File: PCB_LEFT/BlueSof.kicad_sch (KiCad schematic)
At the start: 88 parts, among them J1 USB_C_Receptacle_USB2.0, J12 SM02B-SRSS-TB(LF)(SN), Q2 A03407, SW1 SW_PUSH, SW10 SW_PUSH, SW11 SW_PUSH, SW12 SW_PUSH, SW13 SW_PUSH, SW14 SW_PUSH, SW15 SW_PUSH, SW16 SW_PUSH, SW17 SW_PUSH, SW18 SW_PUSH, SW19 SW_PUSH, SW2 SW_PUSH, SW20 SW_PUSH, SW21 SW_PUSH, SW22 SW_PUSH, SW23 SW_PUSH, SW24 SW_PUSH, SW25 Rotary_Encoder_Switch, SW26 SW_PUSH, SW27 SW_PUSH, SW28 SW_PUSH, SW3 SW_PUSH, SW4 SW_PUSH, SW5 SW_PUSH, SW6 SW_PUSH, SW7 SW_PUSH, SW8 SW_PUSH, SW9 SW_PUSH, U1 LN2054Y42AMR, U2 E73-2G4M08S1C, U3 AP2112K-3.3, Y1 32.768kHz

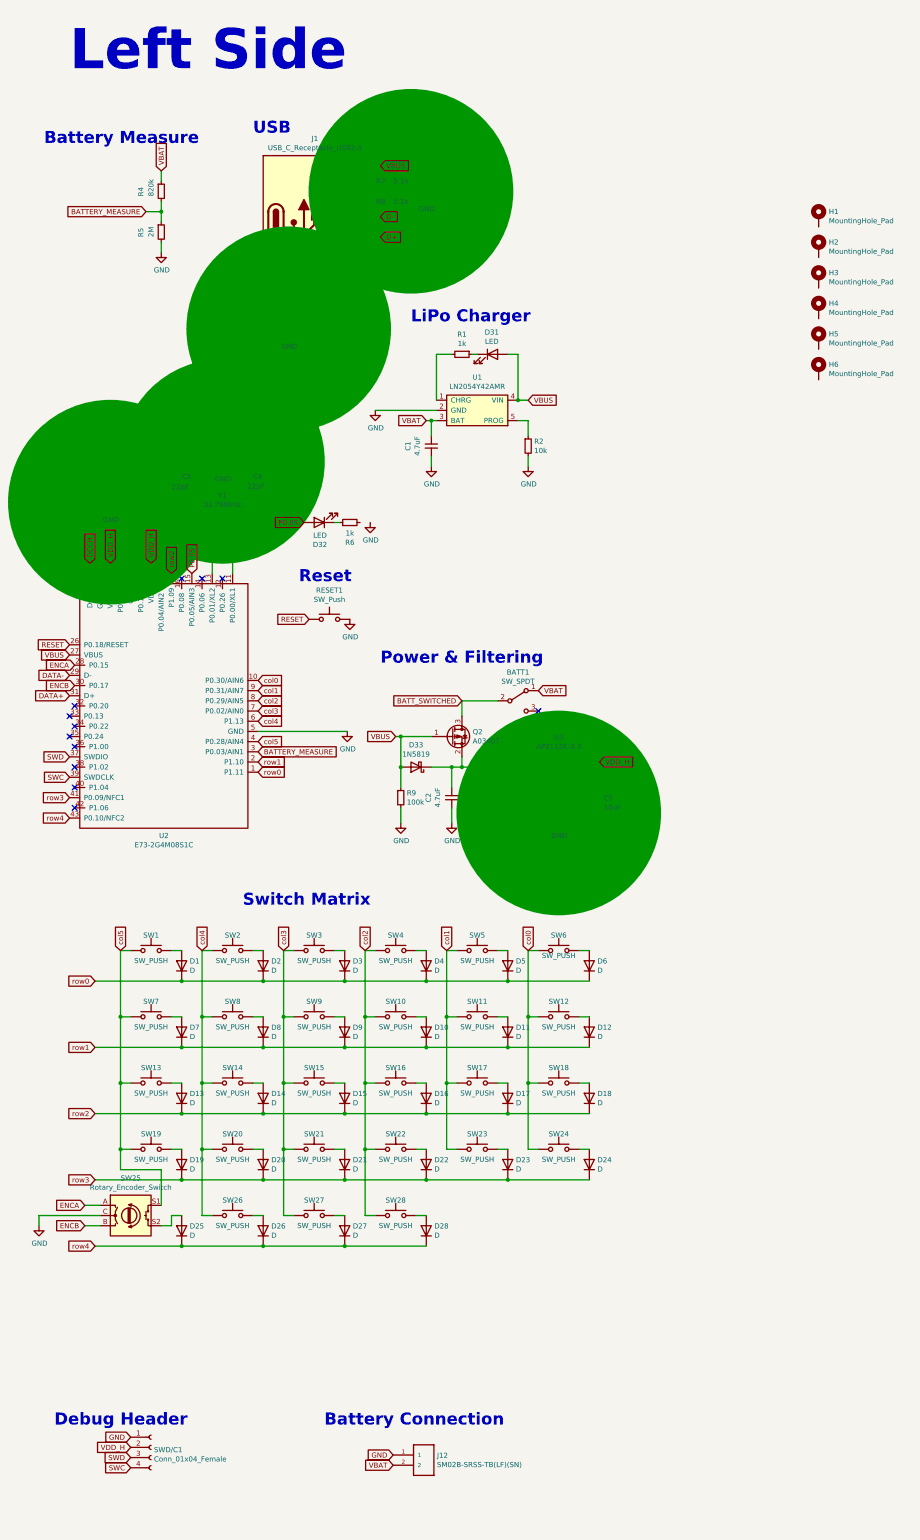
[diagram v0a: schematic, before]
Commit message: ordered left side from jlc
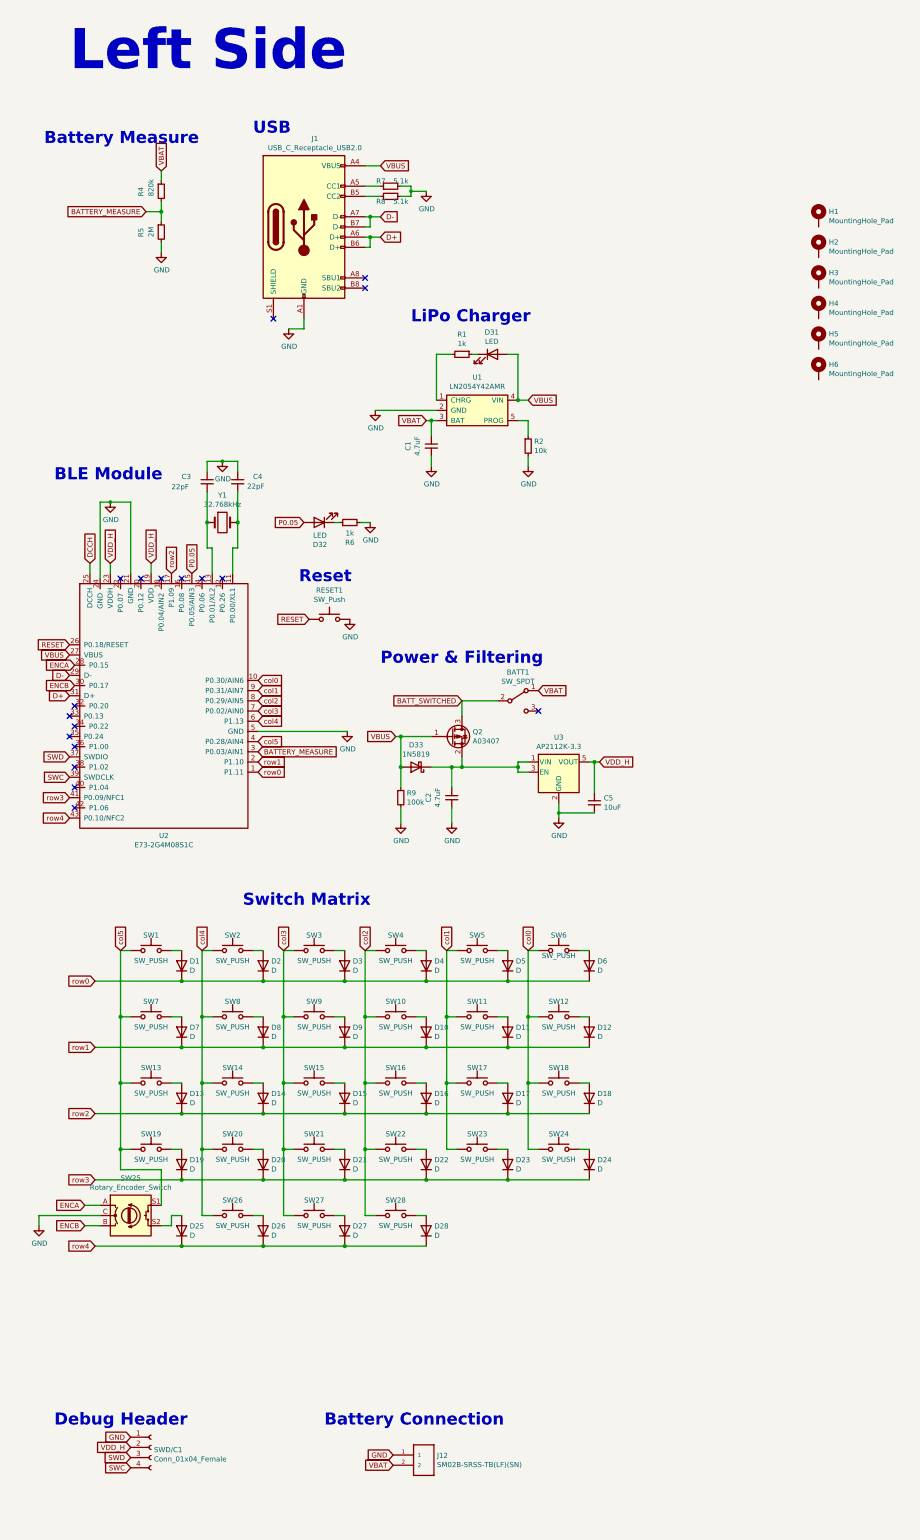
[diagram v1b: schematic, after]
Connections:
- net DATA+ is gone; now on net D+: U2.31 (D+)
- net DATA- is gone; now on net D-: U2.29 (D-)
- net GND: now also R6.2; no longer J1.S1 (SHIELD)
- no-connect marks 17 -> 18
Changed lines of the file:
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@@
     (rev "R1")
   )
-  (junction (at 325.12 146.05) (diameter 50.9956) (color 0 0 0 0))
+  (junction (at 325.12 146.05) (diameter 0.9144) (color 0 0 0 0))
   (junction (at 327.66 274.32) (diameter 1.016) (color 0 0 0 0))
   (junction (at 327.66 290.83) (diameter 1.016) (color 0 0 0 0))
@@
   (junction (at 347.98 307.34) (diameter 1.016) (color 0 0 0 0))
   (junction (at 349.25 151.13) (diameter 1.016) (color 0 0 0 0))
-  (junction (at 353.06 135.89) (diameter 50.9956) (color 0 0 0 0))
+  (junction (at 353.06 135.89) (diameter 0.9144) (color 0 0 0 0))
   (junction (at 356.87 151.13) (diameter 1.016) (color 0 0 0 0))
   (junction (at 363.22 265.43) (diameter 1.016) (color 0 0 0 0))
@@
   (junction (at 368.3 290.83) (diameter 1.016) (color 0 0 0 0))
   (junction (at 368.3 307.34) (diameter 1.016) (color 0 0 0 0))
-  (junction (at 369.57 102.87) (diameter 51) (color 0 0 0 0))
   (junction (at 383.54 265.43) (diameter 1.016) (color 0 0 0 0))
   (junction (at 383.54 281.94) (diameter 1.016) (color 0 0 0 0))
@@
   (junction (at 397.51 204.47) (diameter 1.016) (color 0 0 0 0))
   (junction (at 397.51 212.09) (diameter 1.016) (color 0 0 0 0))
-  (junction (at 400.05 68.58) (diameter 51) (color 0 0 0 0))
+  (junction (at 400.05 68.58) (diameter 0.9144) (color 0 0 0 0))
   (junction (at 403.86 265.43) (diameter 1.016) (color 0 0 0 0))
   (junction (at 403.86 281.94) (diameter 1.016) (color 0 0 0 0))
@@
   (junction (at 429.26 274.32) (diameter 1.016) (color 0 0 0 0))
   (junction (at 429.26 290.83) (diameter 1.016) (color 0 0 0 0))
-  (junction (at 436.88 223.52) (diameter 50.9956) (color 0 0 0 0))
+  (junction (at 436.88 223.52) (diameter 0.9144) (color 0 0 0 0))
   (junction (at 445.77 210.82) (diameter 1.016) (color 0 0 0 0))
   (no_connect (at 314.96 199.39))
@@
   (no_connect (at 347.98 165.1))
   (no_connect (at 353.06 165.1))
+  (no_connect (at 365.76 100.33))
   (no_connect (at 388.62 90.17))
   (no_connect (at 388.62 92.71))
@@
     (stroke (width 0) (type solid) (color 0 0 0 0))
   )
-  (wire (pts (xy 365.76 100.33) (xy 365.76 102.87))
-    (stroke (width 0) (type solid) (color 0 0 0 0))
-  )
-  (wire (pts (xy 365.76 102.87) (xy 369.57 102.87))
-    (stroke (width 0) (type solid) (color 0 0 0 0))
-  )
   (wire (pts (xy 368.3 257.81) (xy 368.3 274.32))
     (stroke (width 0) (type solid) (color 0 0 0 0))
@@
   )
   (wire (pts (xy 383.54 331.47) (xy 403.86 331.47))
+    (stroke (width 0) (type solid) (color 0 0 0 0))
+  )
+  (wire (pts (xy 387.35 151.13) (xy 389.89 151.13))
     (stroke (width 0) (type solid) (color 0 0 0 0))
   )
@@
     (effects (font (size 1.27 1.27)) (justify right))
   )
-  (global_label "DATA-" (shape input) (at 314.96 189.23 180)    (property "Intersheet References" "${INTERSHEET_REFS}" (id 0) (at 95.25 -6.35 0)
-      (effects (font (size 1.27 1.27)) hide)
+  (global_label "D-" (shape input) (at 314.96 189.23 180)    (property "Intersheet References" "${INTERSHEET_REFS}" (id 0) (at 308.1805 189.1506 0)
+      (effects (font (size 1.27 1.27)) (justify right) hide)
     )
     (effects (font (size 1.27 1.27)) (justify right))
   )
-  (global_label "DATA+" (shape input) (at 314.96 194.31 180)    (property "Intersheet References" "${INTERSHEET_REFS}" (id 0) (at 95.25 -6.35 0)
-      (effects (font (size 1.27 1.27)) hide)
+  (global_label "D+" (shape input) (at 314.96 194.31 180)    (property "Intersheet References" "${INTERSHEET_REFS}" (id 0) (at 308.1805 194.2306 0)
+      (effects (font (size 1.27 1.27)) (justify right) hide)
     )
     (effects (font (size 1.27 1.27)) (justify right))

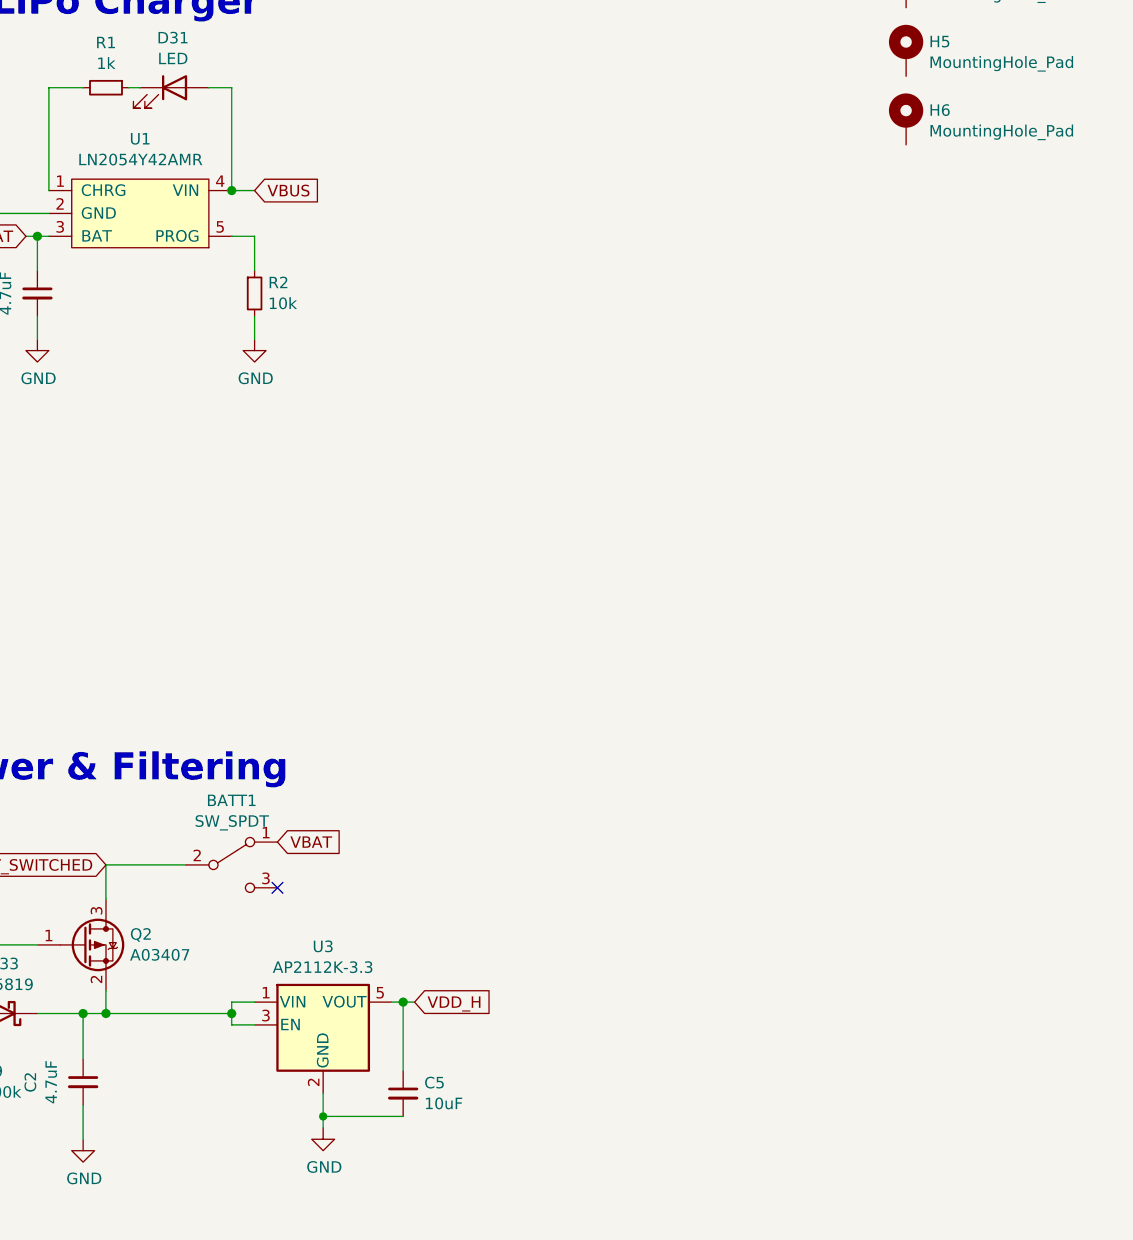
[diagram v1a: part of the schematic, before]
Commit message: minor updates for SMD assembly
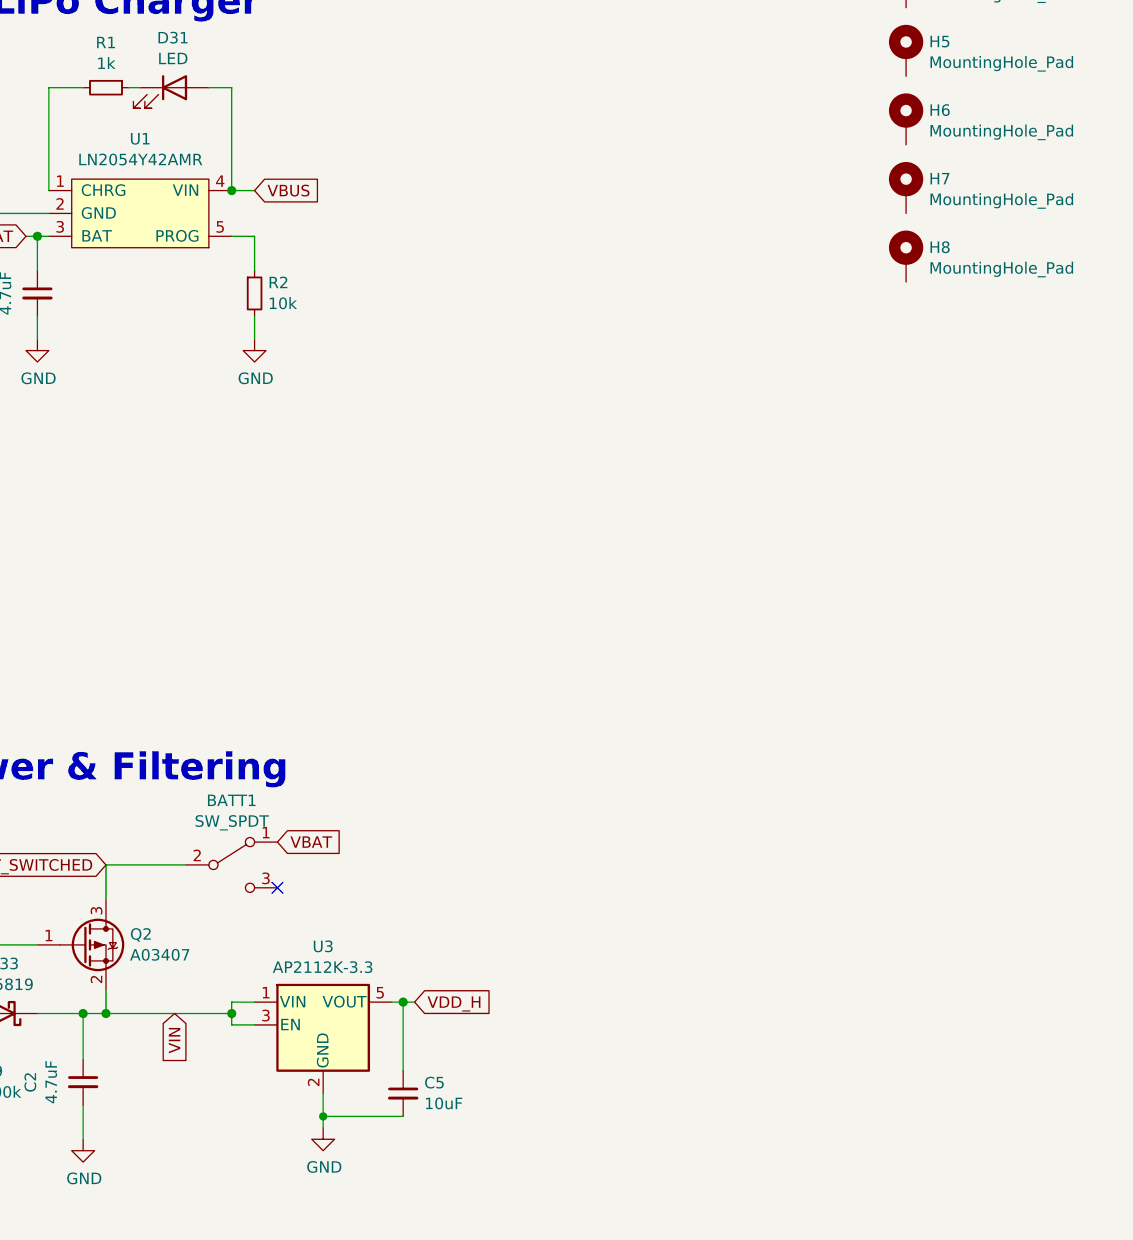
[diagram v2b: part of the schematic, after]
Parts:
- added H7, H8: MountingHole_Pad, MountingHole:MountingHole_4.3mm_M4, symbol Mechanical:MountingHole_Pad
- BATT1: LCSC_PN (none) -> C431540
- C1, C2: LCSC_PN (none) -> C19666
- C3, C4: LCSC_PN (none) -> C1653
- C5: LCSC_PN (none) -> C87152
- D1, D10, D11, D12, D13, D14, D15, D16, D17, D18, D19, D2, D20, D21, D22, D23, D24, D25, D26, D27, D28, D3, D4, D5, D6, D7, D8, D9: LCSC_PN (none) -> C402213
- D33: LCSC_PN (none) -> C489147
- J1: LCSC_PN (none) -> C168688r
- J12: LCSC_PN (none) -> C160402
- Q2: LCSC_PN (none) -> C351408
- R1, R6: LCSC_PN (none) -> C22548
- R2: LCSC_PN (none) -> C98220
- R4: LCSC_PN (none) -> C23252
- R5: LCSC_PN (none) -> C177282
- R7, R8: LCSC_PN (none) -> C105580
- R9: LCSC_PN (none) -> C14675
- RESET1: LCSC_PN (none) -> C231329
- U1: LCSC_PN (none) -> C141406
- U2: footprint BlueSof:E73-2G4M08S1C-52840_minimal_inside_pads -> BlueSof:E73-2G4M08S1C-52840_SMD; LCSC_PN (none) -> C356849
- U3: LCSC_PN (none) -> C51118
- Y1: LCSC_PN (none) -> C93230
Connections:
- net VIN: now reaches C2.1, D33.1 (K), Q2.2 (S), U3.1 (VIN), U3.3 (EN)

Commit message: working towards next order
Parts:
- added BattJumper1: Jumper_2_Open, Jumper:SolderJumper-2_P1.3mm_Open_Pad1.0x1.5mm, symbol Jumper:Jumper_2_Open
- added J2, J3: Conn_01x01_Male, Connector_PinSocket_1.27mm:PinSocket_1x01_P1.27mm_Vertical, symbol Connector:Conn_01x01_Male
- C1, C2, C3, C4, C5: footprint Capacitor_SMD:C_0603_1608Metric_Pad1.08x0.95mm_HandSolder -> Capacitor_SMD:C_0603_1608Metric
- D31, D32: footprint LED_SMD:LED_0603_1608Metric_Pad1.05x0.95mm_HandSolder -> LED_SMD:LED_0603_1608Metric
- R1, R2, R4, R5, R6, R7, R8, R9: footprint Resistor_SMD:R_0603_1608Metric_Pad0.98x0.95mm_HandSolder -> Resistor_SMD:R_0603_1608Metric
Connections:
- net GND: now also J2.1 (Pin_1)
- net VBAT: now also BattJumper1.1 (A)
- new net: BattJumper1.2 (B), J3.1 (Pin_1)
